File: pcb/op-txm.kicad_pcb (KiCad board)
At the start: 2 copper layers, 35 x 85 mm, 56 parts

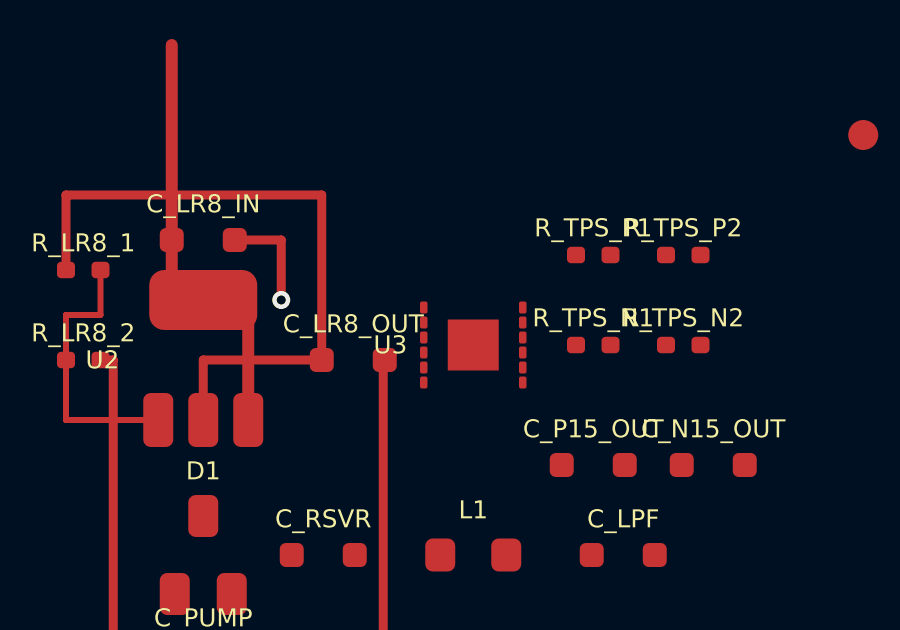
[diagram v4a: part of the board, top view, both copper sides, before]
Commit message: pcb: Task G2 — P15V and N15V outputs from TPS7A3901
P15V (p9) south-detours below the P48V_LDO bottom trunk then runs north
to R_TPS_P1. N15V (p4) exits west then north, sharing the Y=107 corridor
east to R_TPS_N1. Also shifts G1 east drop from X=102.0→102.5 to clear
the P15V westward segment.

Co-Authored-By: Claude Sonnet 4.6 <noreply@anthropic.com>
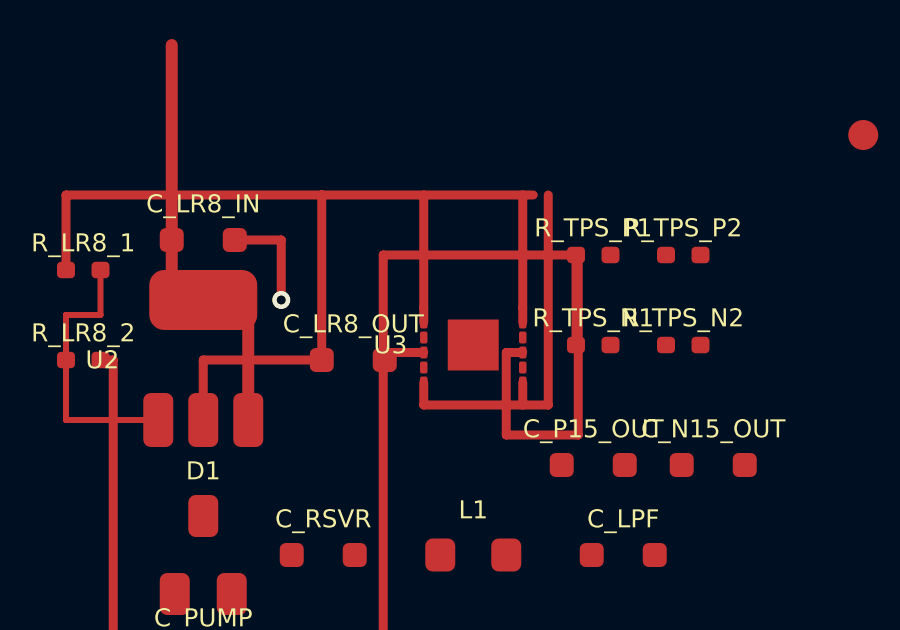
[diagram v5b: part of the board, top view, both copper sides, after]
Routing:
- net P48V_LDO: track 22.5 -> 50.7 mm
- net N15V: track 0.00 -> 14.0 mm
- net P15V: track 0.00 -> 11.8 mm
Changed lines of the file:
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@@
   (segment (start 97.0 110.5) (end 97.0 121.0) (width 0.3) (layer "F.Cu") (net 1))
   (segment (start 97.0 121.0) (end 100.0 121.0) (width 0.3) (layer "F.Cu") (net 1))
+  (segment (start 94.95 105.0) (end 102.0 105.0) (width 0.3) (layer "F.Cu") (net 12))
+  (segment (start 98.35 105.0) (end 98.35 108.75) (width 0.3) (layer "F.Cu") (net 12))
+  (segment (start 98.35 108.75) (end 98.35 109.25) (width 0.3) (layer "F.Cu") (net 12))
+  (segment (start 101.65 105.0) (end 101.65 108.75) (width 0.3) (layer "F.Cu") (net 12))
+  (segment (start 101.65 108.75) (end 101.65 109.25) (width 0.3) (layer "F.Cu") (net 12))
+  (segment (start 102.5 105.0) (end 102.5 112.0) (width 0.3) (layer "F.Cu") (net 12))
+  (segment (start 102.5 112.0) (end 98.35 112.0) (width 0.3) (layer "F.Cu") (net 12))
+  (segment (start 98.35 112.0) (end 98.35 111.25) (width 0.3) (layer "F.Cu") (net 12))
+  (segment (start 101.65 112.0) (end 101.65 111.25) (width 0.3) (layer "F.Cu") (net 12))
+  (segment (start 101.65 110.25) (end 101.1 110.25) (width 0.3) (layer "F.Cu") (net 4))
+  (segment (start 101.1 110.25) (end 101.1 113.0) (width 0.3) (layer "F.Cu") (net 4))
+  (segment (start 101.1 113.0) (end 103.5 113.0) (width 0.3) (layer "F.Cu") (net 4))
+  (segment (start 103.5 113.0) (end 103.5 107.0) (width 0.3) (layer "F.Cu") (net 4))
+  (segment (start 103.5 107.0) (end 103.425 107.0) (width 0.3) (layer "F.Cu") (net 4))
+  (segment (start 98.35 110.25) (end 97.0 110.25) (width 0.3) (layer "F.Cu") (net 5))
+  (segment (start 97.0 110.25) (end 97.0 107.0) (width 0.3) (layer "F.Cu") (net 5))
+  (segment (start 97.0 107.0) (end 103.425 107.0) (width 0.3) (layer "F.Cu") (net 5))
+  (segment (start 103.425 107.0) (end 103.425 110.0) (width 0.3) (layer "F.Cu") (net 5))
   (via (at 88.0 71.0) (size 0.6) (drill 0.3) (layers "F.Cu" "B.Cu") (net 1))
   (via (at 100.0 71.0) (size 0.6) (drill 0.3) (layers "F.Cu" "B.Cu") (net 1))
